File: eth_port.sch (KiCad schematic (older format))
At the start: 48 parts, among them J301 8P8C_LED_Shielded, U301 LAN8810

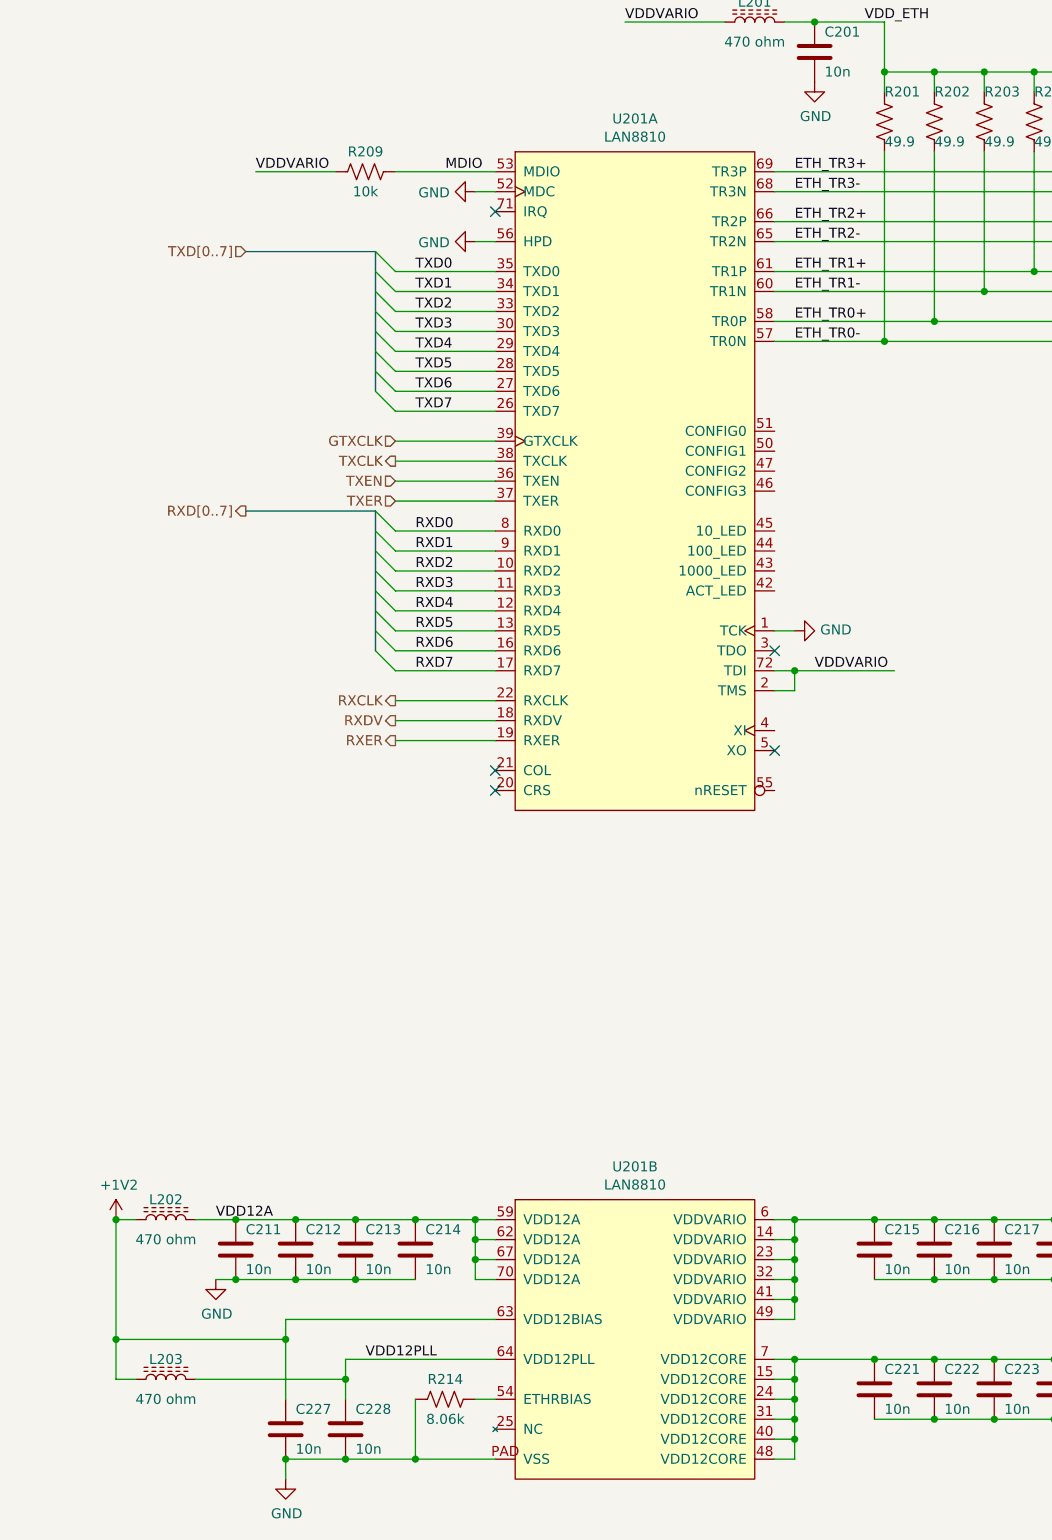
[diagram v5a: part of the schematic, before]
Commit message: Lots of work. - Bussed the two Ethernet blocks together in top level schematic - Mashed Ethernet1 input wires to ground - Added hierarchical label for crystal-in pin - Added a couple more net labels for clarity when routing - Routed Ethernet1 transformer-to-PHY area *including* most of those passives! - Selected a new board shape and started mashing things to fit
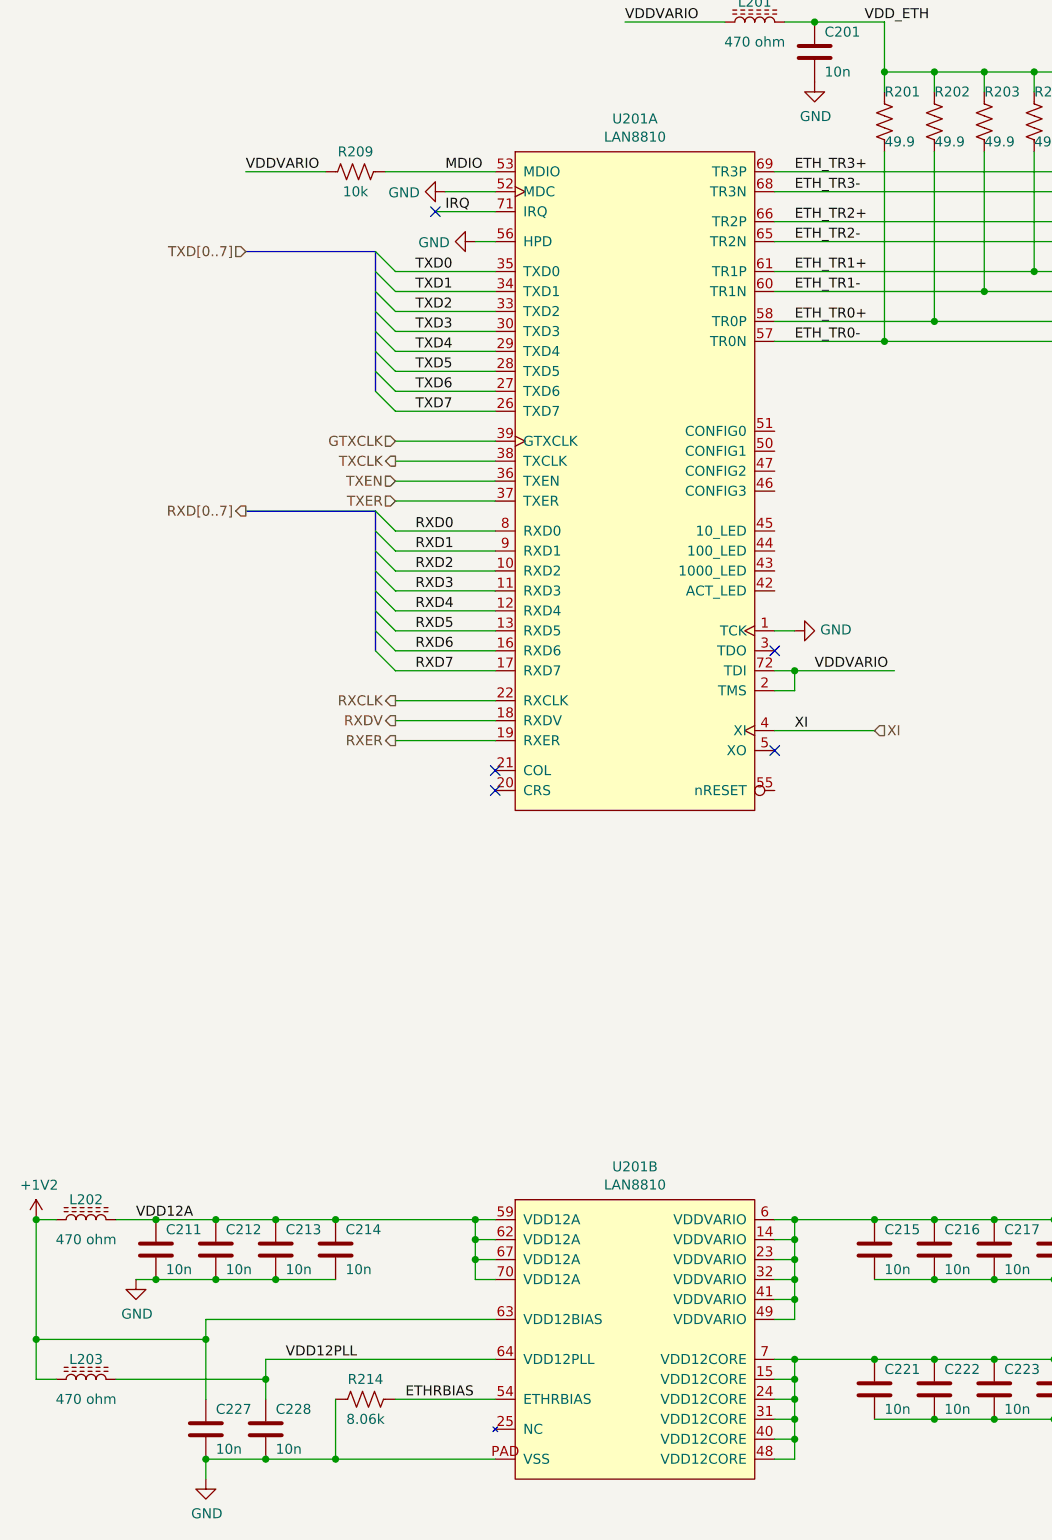
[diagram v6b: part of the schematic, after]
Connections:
- net XI: now reaches U301.4 (XI)
- net IRQ: now reaches U301.71 (IRQ)
- net ETHRBIAS: now reaches R314.1, U301.54 (ETHRBIAS)
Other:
- moved on the sheet: C211, C212, C213, C214, C227, C228, L202, L203, R209, R214

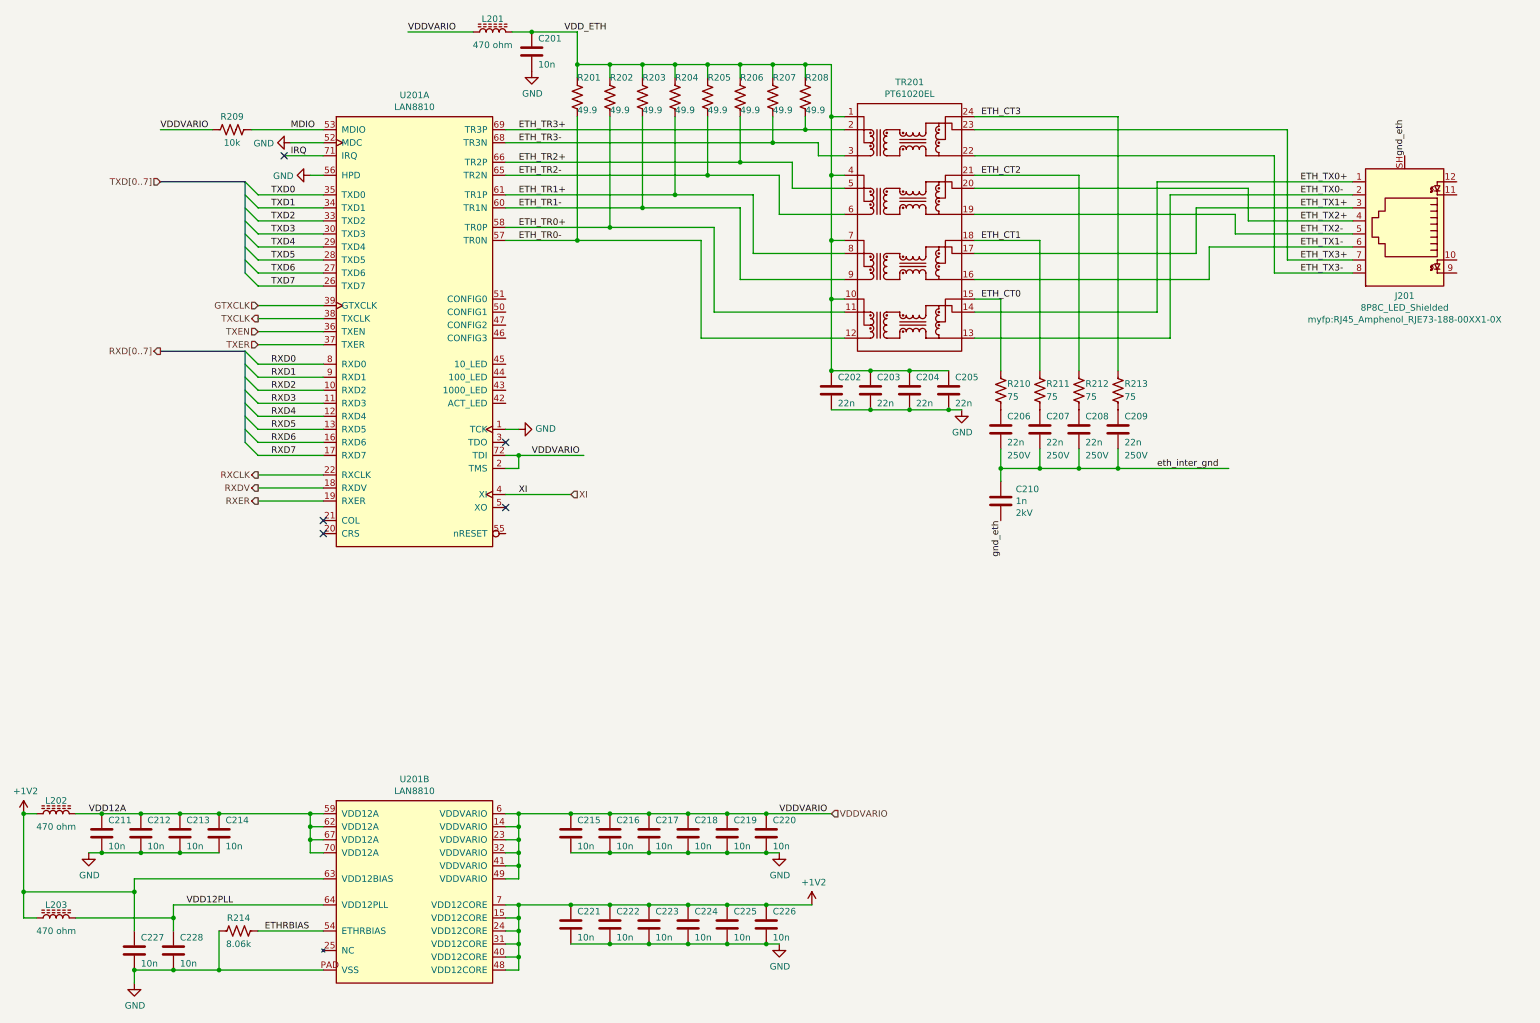
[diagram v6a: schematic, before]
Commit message: - Added copyright and license headers to the schematic - Started in on the power supply, from 0 to 80% or so, including documentation
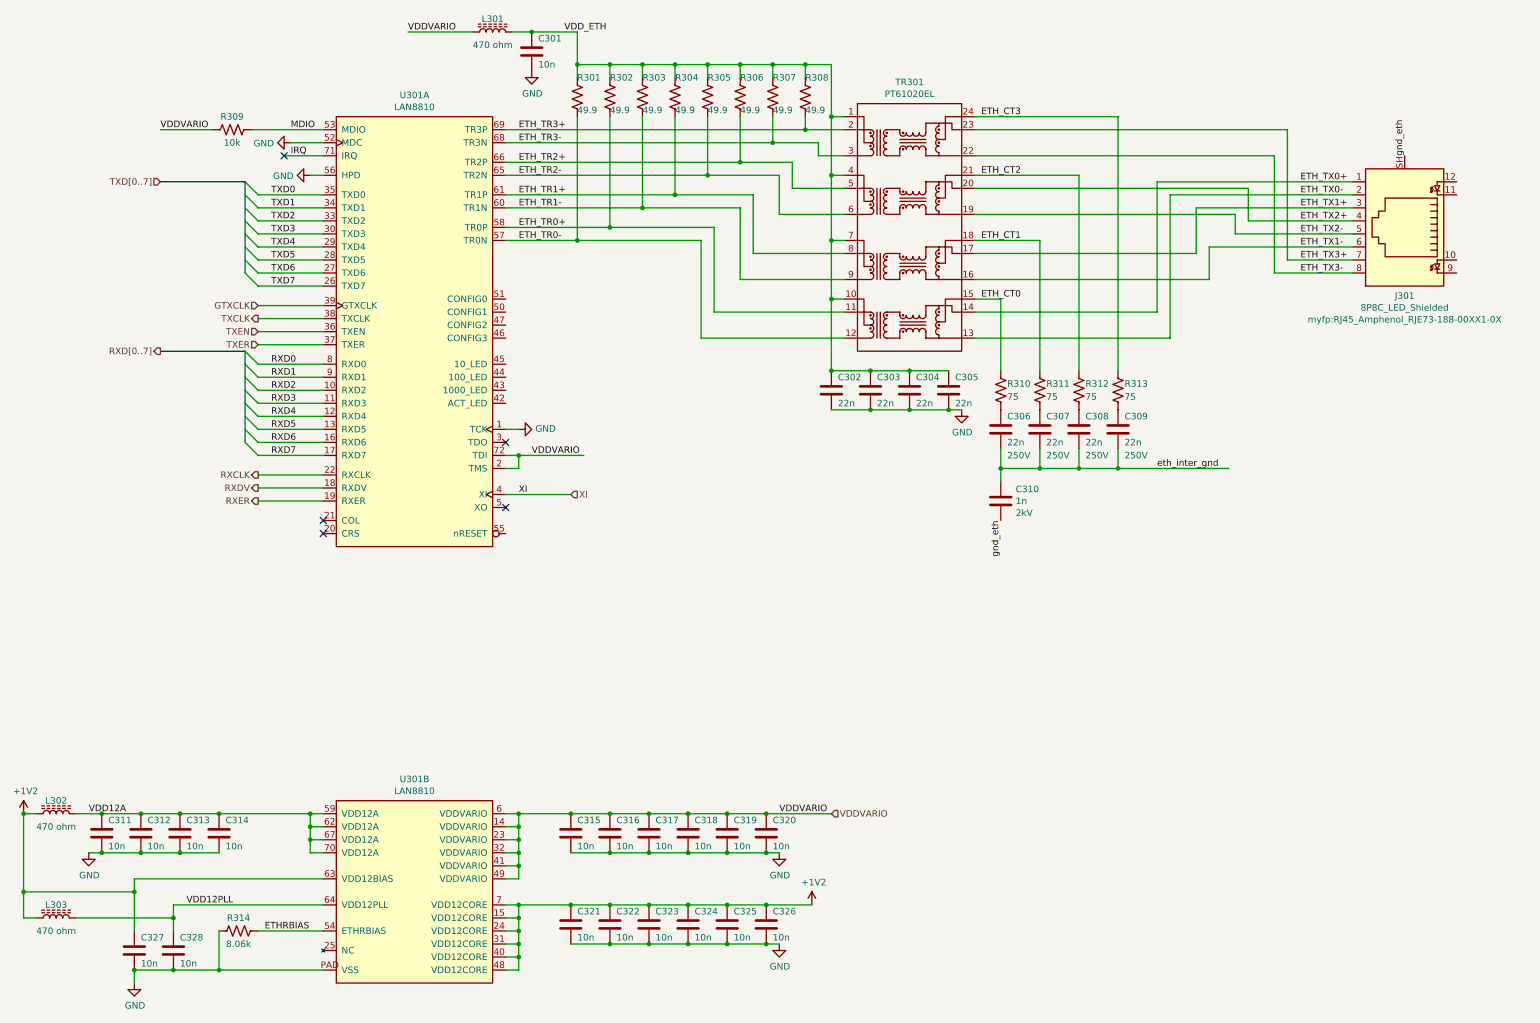
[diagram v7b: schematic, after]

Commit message: Forward progress - Started the real 1.2V power plane - Placed and routed most of PHY1 decoupling capacitors - Placed and partly routed transformer2 PHY-side resistors & capacitors - Labelled a few more nets for clarity during layout
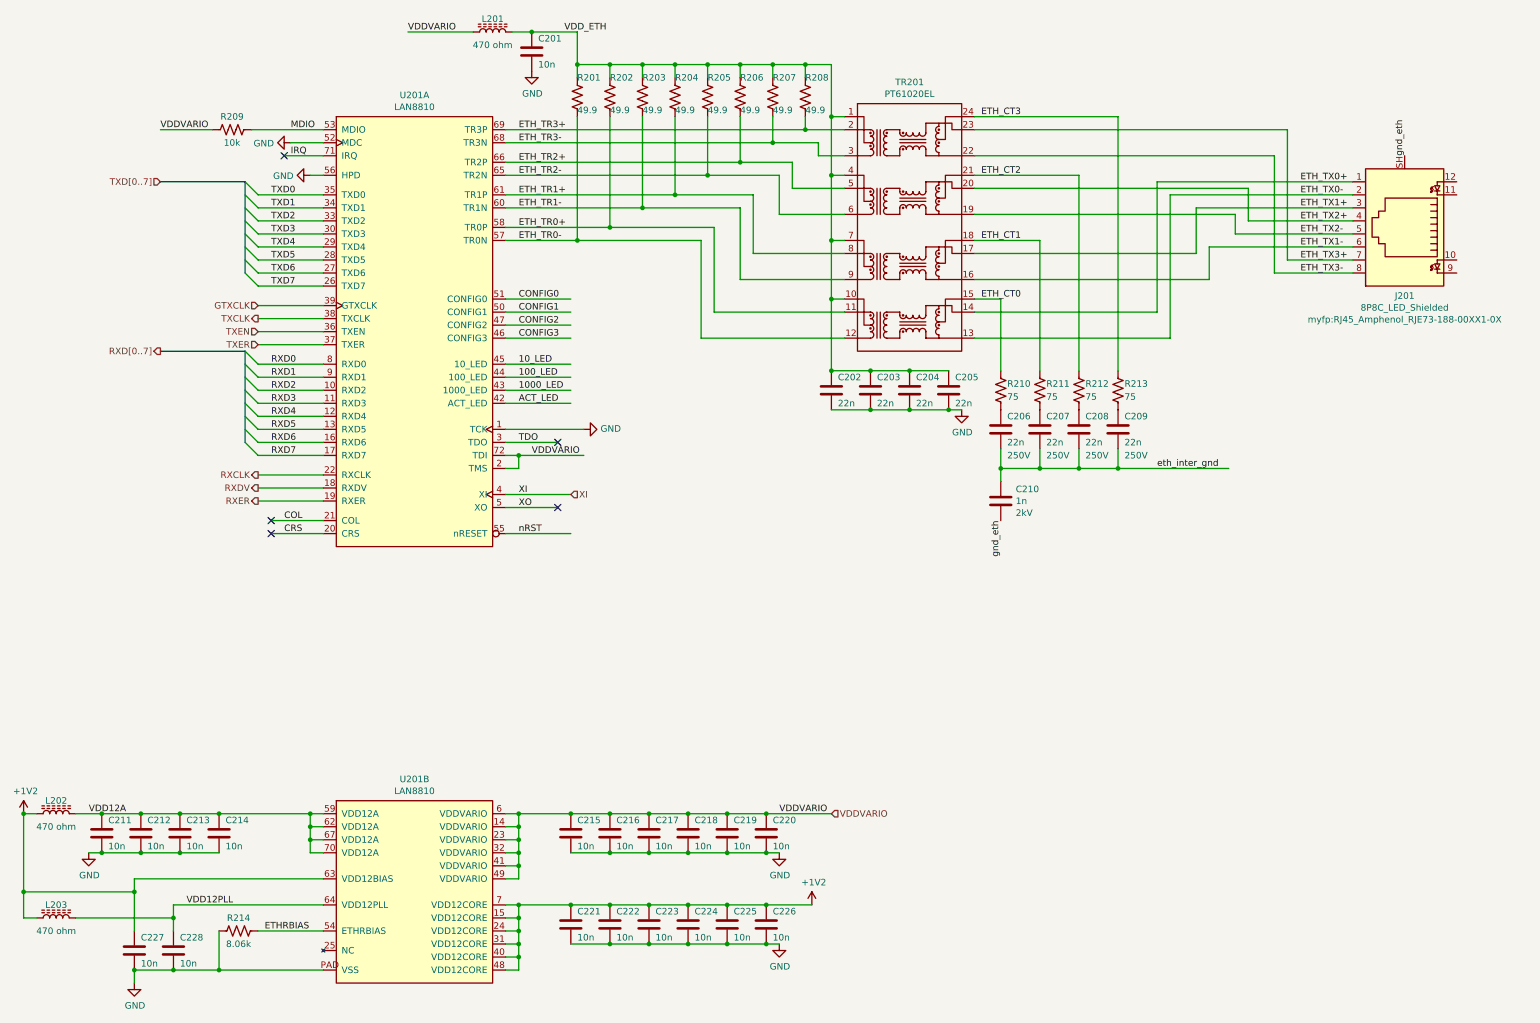
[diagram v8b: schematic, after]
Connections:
- net labels added: 1000_LED, 100_LED, 10_LED, ACT_LED, COL, CONFIG0, CONFIG1, CONFIG2, CONFIG3, CRS, TDO, XO, nRST
- wire segments 231 -> 244
